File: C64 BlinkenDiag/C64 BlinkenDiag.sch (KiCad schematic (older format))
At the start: 7 parts, among them J1 C64-Exp-Port, SW1 Function, SW2 Bank, SW3 RESET, U1 28C256

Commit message: Added switch to disable ROM
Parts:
- added J2: Voltmeter, symbol voltmeter:PWR
- added SW1: ROM_EN, symbol Switch:SW_DPDT_x2
- SW4: renamed from SW3; value RESET -> Reset
- renumbered SW1 to SW2, SW2 to SW3
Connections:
- net A13: now also SW1.4 (A); no longer J1.9 (~EXROM)
- net GND: now also J2.1 (Pin_1)
- net VCC: now also J2.2 (Pin_2)
- net ~GAME: now also SW1.2 (B); no longer SW2.3 (C)
- new net: SW1.1 (A), SW2.3 (C)
- new net ~EXROM: J1.9 (~EXROM), SW1.5 (B)
- no-connect marks 16 -> 18
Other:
- moved on the sheet: R1, R2, SW2A, SW2B, SW3A, SW3B, SW4

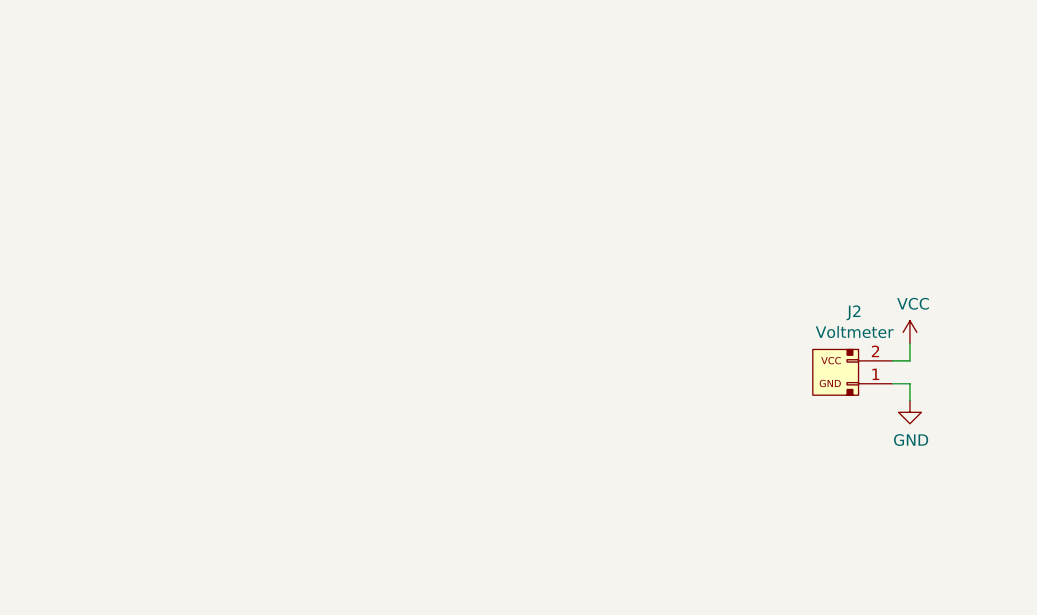
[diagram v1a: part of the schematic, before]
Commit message: Added voltmeter module and mounting library
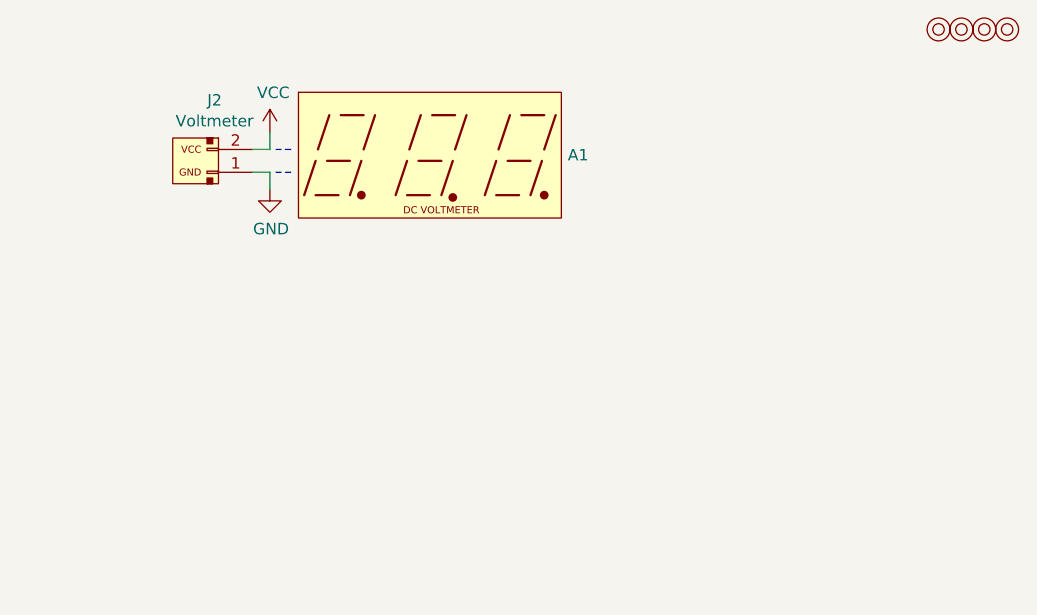
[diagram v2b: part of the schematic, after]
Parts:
- added A1: module, symbol voltmeter:module
- added M1, M2, M3, M4: Mounting, symbol mounting:Mounting
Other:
- moved on the sheet: J2
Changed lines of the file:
@@
 L voltmeter:PWR J2
 U 1 1 605335F3
-P 10375 2050
-F 0 "J2" H 10292 2315 50  0000 C CNN
-F 1 "Voltmeter" H 10292 2224 50  0000 C CNN
-F 2 "" H 10325 2200 50  0001 C CNN
-F 3 "~" H 10325 2200 50  0001 C CNN
-	1    10375 2050
+P 7575 1125
+F 0 "J2" H 7492 1390 50  0000 C CNN
+F 1 "Voltmeter" H 7492 1299 50  0000 C CNN
+F 2 "" H 7525 1275 50  0001 C CNN
+F 3 "~" H 7525 1275 50  0001 C CNN
+	1    7575 1125
 	-1   0    0    -1
 $EndComp
@@
 L power:VCC #PWR0111
 U 1 1 605398EE
-P 10700 1925
-F 0 "#PWR0111" H 10700 1775 50  0001 C CNN
-F 1 "VCC" H 10715 2098 50  0000 C CNN
-F 2 "" H 10700 1925 50  0001 C CNN
-F 3 "" H 10700 1925 50  0001 C CNN
-	1    10700 1925
+P 7900 1000
+F 0 "#PWR0111" H 7900 850 50  0001 C CNN
+F 1 "VCC" H 7915 1173 50  0000 C CNN
+F 2 "" H 7900 1000 50  0001 C CNN
+F 3 "" H 7900 1000 50  0001 C CNN
+	1    7900 1000
 	1    0    0    -1
 $EndComp
 Wire Wire Line
-	10700 1925 10700 2000
+	7900 1000 7900 1075
 Wire Wire Line
-	10700 2000 10625 2000
+	7900 1075 7825 1075
 Wire Wire Line
-	10625 2100 10700 2100
+	7825 1175 7900 1175
 Wire Wire Line
-	10700 2100 10700 2175
+	7900 1175 7900 1250
 $Comp
 L power:GND #PWR0112
 U 1 1 6054483A
-P 10700 2175
-F 0 "#PWR0112" H 10700 1925 50  0001 C CNN
-F 1 "GND" H 10705 2002 50  0000 C CNN
-F 2 "" H 10700 2175 50  0001 C CNN
-F 3 "" H 10700 2175 50  0001 C CNN
-	1    10700 2175
+P 7900 1250
+F 0 "#PWR0112" H 7900 1000 50  0001 C CNN
+F 1 "GND" H 7905 1077 50  0000 C CNN
+F 2 "" H 7900 1250 50  0001 C CNN
+F 3 "" H 7900 1250 50  0001 C CNN
+	1    7900 1250
 	1    0    0    -1
 $EndComp
+$Comp
+L mounting:Mounting M1
+U 1 1 60580700
+P 10825 550
+F 0 "M1" H 10825 650 50  0001 C CNN
+F 1 "Mounting" H 10825 475 50  0001 C CNN
+F 2 "" H 10825 550 50  0001 C CNN
+F 3 "~" H 10825 550 50  0001 C CNN
+	1    10825 550
+	1    0    0    -1
+$EndComp
+$Comp
+L mounting:Mounting M2
+U 1 1 60580BA0
+P 10925 550
+F 0 "M2" H 10925 650 50  0001 C CNN
+F 1 "Mounting" H 10925 475 50  0001 C CNN
+F 2 "" H 10925 550 50  0001 C CNN
+F 3 "~" H 10925 550 50  0001 C CNN
+	1    10925 550
+	1    0    0    -1
+$EndComp
+$Comp
+L mounting:Mounting M3
+U 1 1 6058141F
+P 11025 550
+F 0 "M3" H 11025 650 50  0001 C CNN
+F 1 "Mounting" H 11025 475 50  0001 C CNN
+F 2 "" H 11025 550 50  0001 C CNN
+F 3 "~" H 11025 550 50  0001 C CNN
+	1    11025 550
+	1    0    0    -1
+$EndComp
+$Comp
+L mounting:Mounting M4
+U 1 1 60581816
+P 11125 550
+F 0 "M4" H 11125 650 50  0001 C CNN
+F 1 "Mounting" H 11125 475 50  0001 C CNN
+F 2 "" H 11125 550 50  0001 C CNN
+F 3 "~" H 11125 550 50  0001 C CNN
+	1    11125 550
+	1    0    0    -1
+$EndComp
+$Comp
+L voltmeter:module A1
+U 1 1 605A38BF
+P 8625 1075
+F 0 "A1" H 9203 1050 50  0000 L CNN
+F 1 "module" H 8625 800 50  0001 C CNN
+F 2 "" H 8625 1075 50  0001 C CNN
+F 3 "" H 8625 1075 50  0001 C CNN
+	1    8625 1075
+	1    0    0    -1
+$EndComp
+Wire Notes Line
+	7925 1075 8000 1075
+Wire Notes Line
+	7925 1175 8000 1175
 Wire Bus Line
 	5750 2250 5750 4350

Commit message: Assign footprints
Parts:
- J1: footprint MODULE -> C64_Exp_Port:C64_Expansion_Port
- J2: footprint (none) -> Connector_JST:JST_XH_B2B-XH-A_1x02_P2.50mm_Vertical
- M1, M2, M3, M4: footprint (none) -> mounting:M3
- R1, R2: footprint (none) -> Resistor_THT:R_Axial_DIN0207_L6.3mm_D2.5mm_P10.16mm_Horizontal
- SW1, SW2, SW3: footprint (none) -> 6pin_switch:dpdt_switch_black
- SW4: footprint (none) -> switch_cutout:SW_PUSH_6mm
- U1: footprint (none) -> Package_DIP:DIP-28_W15.24mm_Socket_LongPads
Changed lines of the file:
@@
 F 0 "J1" H 2050 3800 50  0000 C CNN
 F 1 "C64-Exp-Port" V 2425 2500 50  0000 C CNN
-F 2 "MODULE" H 2425 1050 50  0001 C CNN
+F 2 "C64_Exp_Port:C64_Expansion_Port" H 2425 1050 50  0001 C CNN
 F 3 "DOCUMENTATION" H 2425 950 50  0001 C CNN
 	1    2425 2500
@@
 F 0 "U1" H 4400 4050 50  0000 C CNN
 F 1 "28C256" V 4725 3050 50  0000 C CNN
-F 2 "" H 4725 3050 50  0001 C CNN
+F 2 "Package_DIP:DIP-28_W15.24mm_Socket_LongPads" H 4725 3050 50  0001 C CNN
 F 3 "memory/28c256.pdf" H 4725 3050 50  0001 C CNN
 	1    4725 3050
@@
 F 0 "SW4" H 4775 1410 50  0000 C CNN
 F 1 "Reset" H 4775 1319 50  0000 C CNN
-F 2 "" H 4775 1325 50  0001 C CNN
+F 2 "switch_cutout:SW_PUSH_6mm" H 4775 1325 50  0001 C CNN
 F 3 "~" H 4775 1325 50  0001 C CNN
 	1    4775 1125
@@
 F 0 "SW2" H 3350 6100 50  0000 C CNN
 F 1 "Function" H 3350 6191 50  0000 C CNN
-F 2 "" H 3350 6425 50  0001 C CNN
+F 2 "6pin_switch:dpdt_switch_black" H 3350 6425 50  0001 C CNN
 F 3 "~" H 3350 6425 50  0001 C CNN
 	2    3350 6425
@@
 F 0 "SW3" H 5025 4975 50  0000 C CNN
 F 1 "Bank" H 5025 5066 50  0000 C CNN
-F 2 "" H 5025 5300 50  0001 C CNN
+F 2 "6pin_switch:dpdt_switch_black" H 5025 5300 50  0001 C CNN
 F 3 "~" H 5025 5300 50  0001 C CNN
 	1    5025 5300
@@
 F 0 "SW3" H 5025 6125 50  0000 C CNN
 F 1 "Bank" H 5025 6216 50  0000 C CNN
-F 2 "" H 5025 6450 50  0001 C CNN
+F 2 "6pin_switch:dpdt_switch_black" H 5025 6450 50  0001 C CNN
 F 3 "~" H 5025 6450 50  0001 C CNN
 	2    5025 6450
@@
 F 0 "R1" H 3870 5471 50  0000 L CNN
 F 1 "10k" H 3870 5380 50  0000 L CNN
-F 2 "" V 3730 5425 50  0001 C CNN
+F 2 "Resistor_THT:R_Axial_DIN0207_L6.3mm_D2.5mm_P10.16mm_Horizontal" V 3730 5425 50  0001 C CNN
 F 3 "~" H 3800 5425 50  0001 C CNN
 	1    3800 5425
@@
 F 0 "R2" H 5545 5471 50  0000 L CNN
 F 1 "10k" H 5545 5380 50  0000 L CNN
-F 2 "" V 5405 5425 50  0001 C CNN
+F 2 "Resistor_THT:R_Axial_DIN0207_L6.3mm_D2.5mm_P10.16mm_Horizontal" V 5405 5425 50  0001 C CNN
 F 3 "~" H 5475 5425 50  0001 C CNN
 	1    5475 5425
@@
 F 0 "SW1" H 2025 4700 50  0000 C CNN
 F 1 "ROM_EN" H 2025 4791 50  0000 C CNN
-F 2 "" H 2025 5025 50  0001 C CNN
+F 2 "6pin_switch:dpdt_switch_black" H 2025 5025 50  0001 C CNN
 F 3 "~" H 2025 5025 50  0001 C CNN
 	1    2025 5025
@@
 F 0 "SW1" H 2025 5425 50  0000 C CNN
 F 1 "ROM_EN" H 2025 5516 50  0000 C CNN
-F 2 "" H 2025 5750 50  0001 C CNN
+F 2 "6pin_switch:dpdt_switch_black" H 2025 5750 50  0001 C CNN
 F 3 "~" H 2025 5750 50  0001 C CNN
 	2    2025 5750
@@
 F 0 "SW2" H 3350 4975 50  0000 C CNN
 F 1 "Function" H 3350 5066 50  0000 C CNN
-F 2 "" H 3350 5300 50  0001 C CNN
+F 2 "6pin_switch:dpdt_switch_black" H 3350 5300 50  0001 C CNN
 F 3 "~" H 3350 5300 50  0001 C CNN
 	1    3350 5300
@@
 F 0 "J2" H 7492 1390 50  0000 C CNN
 F 1 "Voltmeter" H 7492 1299 50  0000 C CNN
-F 2 "" H 7525 1275 50  0001 C CNN
+F 2 "Connector_JST:JST_XH_B2B-XH-A_1x02_P2.50mm_Vertical" H 7525 1275 50  0001 C CNN
 F 3 "~" H 7525 1275 50  0001 C CNN
 	1    7575 1125
@@
 F 0 "M1" H 10825 650 50  0001 C CNN
 F 1 "Mounting" H 10825 475 50  0001 C CNN
-F 2 "" H 10825 550 50  0001 C CNN
+F 2 "mounting:M3" H 10825 550 50  0001 C CNN
 F 3 "~" H 10825 550 50  0001 C CNN
 	1    10825 550
@@
 F 0 "M2" H 10925 650 50  0001 C CNN
 F 1 "Mounting" H 10925 475 50  0001 C CNN
-F 2 "" H 10925 550 50  0001 C CNN
+F 2 "mounting:M3" H 10925 550 50  0001 C CNN
 F 3 "~" H 10925 550 50  0001 C CNN
 	1    10925 550
@@
 F 0 "M3" H 11025 650 50  0001 C CNN
 F 1 "Mounting" H 11025 475 50  0001 C CNN
-F 2 "" H 11025 550 50  0001 C CNN
+F 2 "mounting:M3" H 11025 550 50  0001 C CNN
 F 3 "~" H 11025 550 50  0001 C CNN
 	1    11025 550
@@
 F 0 "M4" H 11125 650 50  0001 C CNN
 F 1 "Mounting" H 11125 475 50  0001 C CNN
-F 2 "" H 11125 550 50  0001 C CNN
+F 2 "mounting:M3" H 11125 550 50  0001 C CNN
 F 3 "~" H 11125 550 50  0001 C CNN
 	1    11125 550
